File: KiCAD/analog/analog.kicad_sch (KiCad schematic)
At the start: 0 parts

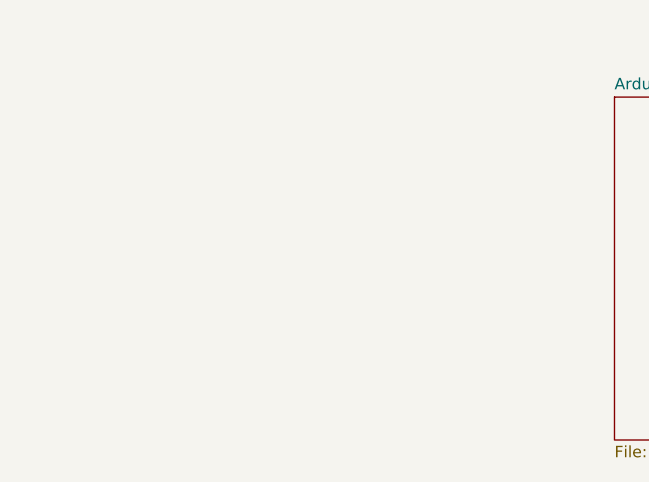
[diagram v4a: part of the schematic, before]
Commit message: revD: U18 heartbeat RC reset + fault_shutdown migrated to analog
- arduino.kicad_sch: R48 10K + C14 10uF RC on U18 RST_A holds
  CD14538B heartbeat watchdog in reset ~70-120ms during Metro boot,
  preventing SS_PWR_RLY / SS_PA_INRUSH false-energize while PCF8575
  defaults HIGH on its outputs
- fault_shutdown.kicad_sch (new): LM393 overcurrent trip +
  CD74HC4066 bias switch + V_REF latch migrated from ss_pa to
  analog so FAULT_N stays off the umbilical; co-located with the
  Metro that reads it. Ref numbers +200 to avoid collision with
  pre-existing analog refs
- analog.kicad_sch: adds Fault_Shutdown sub-sheet reference (page 11)
- ss_pa: fault_shutdown sheet reference removed; ss_pa.net reflects
  the component loss (eliminates ss_pa U3 LM2936 LDO and +5V rail
  dependency)
- pa_stage.kicad_sch: R1-R4 bumped to 2W (RSF200JT-73-0R22) with
  DIN0516 L15.5mm footprint; footprint cleanup pass
- power.kicad_sch: 4.7R dummy bumped to 4.7R 10W with Axial_Power
  L25.0mm W9.0mm P30.48mm footprint

Co-Authored-By: Claude Opus 4.7 <noreply@anthropic.com>
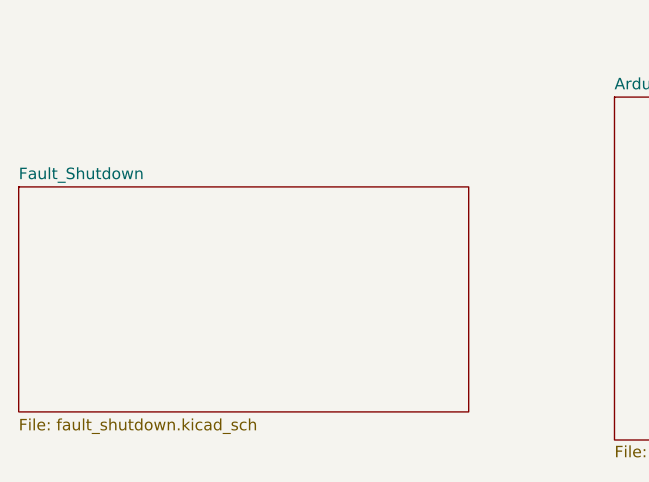
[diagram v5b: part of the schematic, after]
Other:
- added sheet Fault_Shutdown (fault_shutdown.kicad_sch)
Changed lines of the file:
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@@
+	)
+	(sheet
+		(at 23.97 116.66)
+		(size 50 25)
+		(exclude_from_sim no)
+		(in_bom yes)
+		(on_board yes)
+		(dnp no)
+		(fields_autoplaced yes)
+		(stroke
+			(width 0.1524)
+			(type solid)
+		)
+		(fill
+			(color 0 0 0 0)
+		)
+		(property "Sheetname" "Fault_Shutdown"
+			(at 23.97 115.9484 0)
+			(show_name no)
+			(do_not_autoplace no)
+			(effects
+				(font
+					(size 1.27 1.27)
+				)
+				(justify left bottom)
+			)
+		)
+		(property "Sheetfile" "fault_shutdown.kicad_sch"
+			(at 23.97 142.3746 0)
+			(show_name no)
+			(do_not_autoplace no)
+			(effects
+				(font
+					(size 1.27 1.27)
+				)
+				(justify left top)
+			)
+		)
+		(instances
+			(project "analog"
+				(path "/d3de40b8-856b-4fbd-829c-f45ffcd55742"
+					(page "11")
+				)
+			)
+		)
 	)
 	(sheet

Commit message: revD: front panel absorbed into analog as sub-sheet
- front_panel.kicad_sch (new): front-panel circuitry pulled onto
  the analog board as a hierarchical sub-sheet; eliminates the
  separate frontpanel PCB (board count now 3: analog, ss_pa,
  Output LPF)
- analog.kicad_sch: new sub-sheet reference for Front_Panel
- interface.kicad_sch: rewired to connect to the local
  Front_Panel sheet instead of the former RJ45 umbilical
- analog.net regenerated

NOTE: KiCAD/frontpanel/ directory still present on disk; will be
removed in a later cleanup commit once the absorbed version is
verified ERC-clean.

Co-Authored-By: Claude Opus 4.7 <noreply@anthropic.com>
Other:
- added sheet Front_Panel (front_panel.kicad_sch)
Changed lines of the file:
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@@
 	(paper "A4")
+	(sheet
+		(at 73.66 167.64)
+		(size 35.56 17.78)
+		(exclude_from_sim no)
+		(in_bom yes)
+		(on_board yes)
+		(dnp no)
+		(fields_autoplaced yes)
+		(stroke
+			(width 0.1524)
+			(type solid)
+		)
+		(fill
+			(color 0 0 0 0)
+		)
+		(property "Sheetname" "Front_Panel"
+			(at 73.66 166.9284 0)
+			(show_name no)
+			(do_not_autoplace no)
+			(effects
+				(font
+					(size 1.27 1.27)
+				)
+				(justify left bottom)
+			)
+		)
+		(property "Sheetfile" "front_panel.kicad_sch"
+			(at 73.66 186.0046 0)
+			(show_name no)
+			(do_not_autoplace no)
+			(effects
+				(font
+					(size 1.27 1.27)
+				)
+				(justify left top)
+			)
+		)
+		(instances
+			(project "analog"
+				(path "/d3de40b8-856b-4fbd-829c-f45ffcd55742"
+					(page "4")
+				)
+			)
+		)
+	)
 	(sheet
 		(at 90.17 106.68)
